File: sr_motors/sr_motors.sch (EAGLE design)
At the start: 20 parts

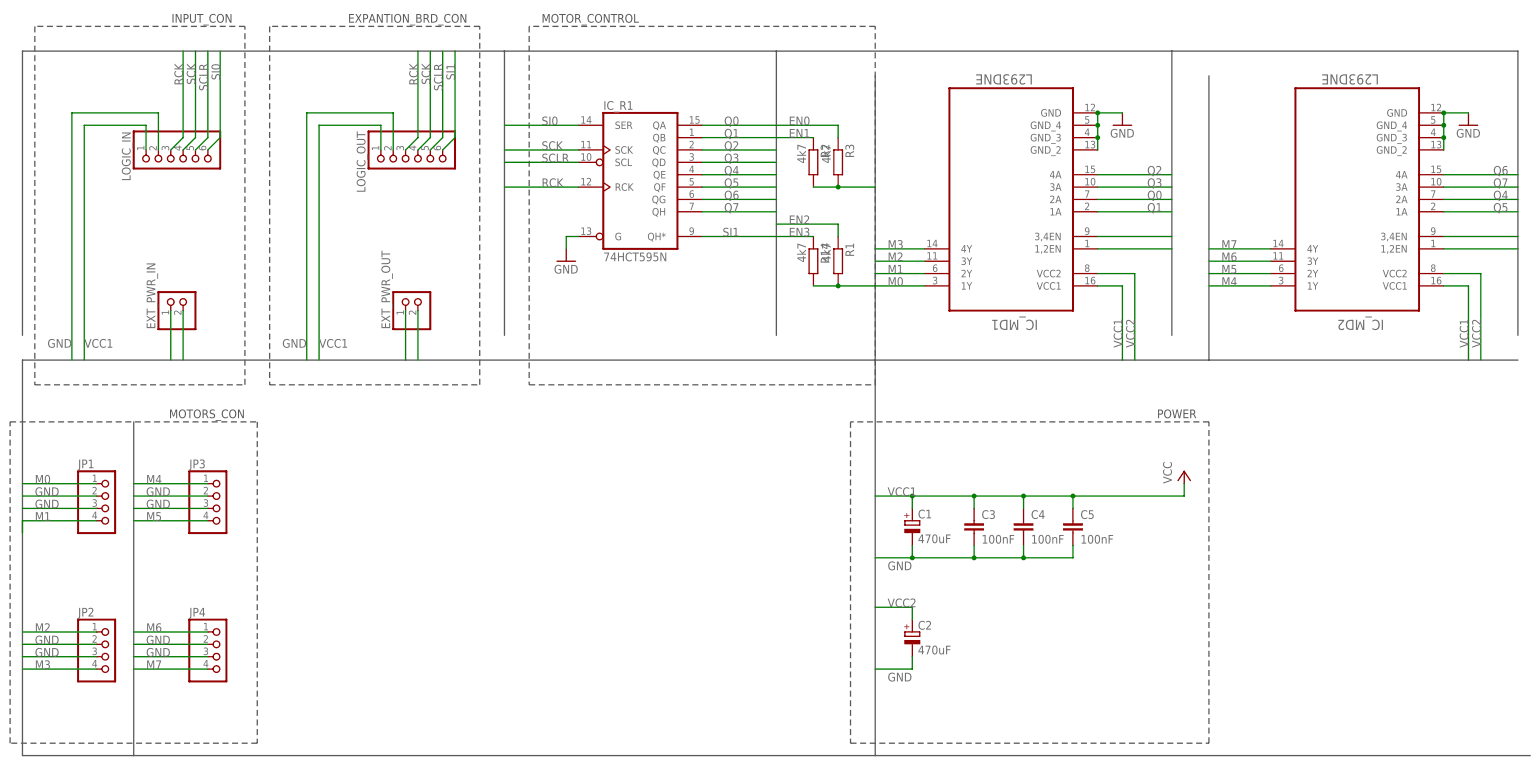
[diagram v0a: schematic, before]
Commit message: Added reverse current protection for external power, added version text
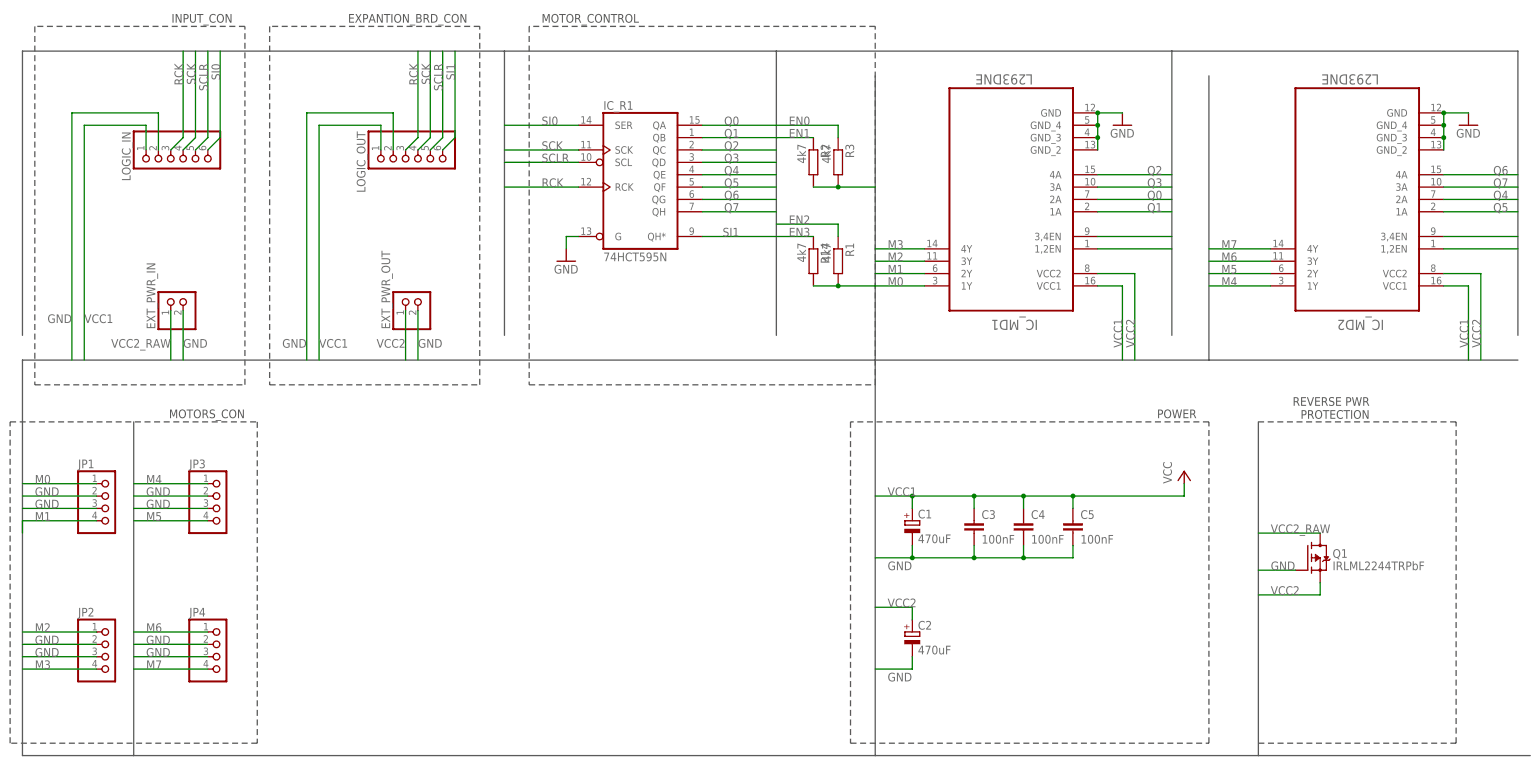
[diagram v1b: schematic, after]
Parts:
- added Q1: IRLML2244TRPbF, we-transistor:MOSFET-P-SOT23
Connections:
- new net VCC2_RAW: EXT_PWR_IN.1, Q1.D
- net GND: now also Q1.G
- net VCC2: now also Q1.S; no longer EXT_PWR_IN.1
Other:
- note added: "REVERSE PWR PROTECTION"
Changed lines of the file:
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@@
 <part name="JP3" library="pinhead" deviceset="PINHD-1X4" device=""/>
 <part name="JP4" library="pinhead" deviceset="PINHD-1X4" device=""/>
+<part name="Q1" library="we-transistor" deviceset="MOSFET-P" device="-SOT23" value="IRLML2244TRPbF"/>
 </parts>
 <sheets>
@@
 <text x="104.14" y="149.86" size="1.778" layer="97" rot="MR180">MOTOR_CONTROL</text>
 <text x="43.18" y="68.58" size="1.778" layer="97" rot="R180">MOTORS_CON</text>
+<wire x1="251.46" y1="0" x2="292.1" y2="0" width="0.1524" layer="97" style="shortdash"/>
+<wire x1="292.1" y1="0" x2="292.1" y2="66.04" width="0.1524" layer="97" style="shortdash"/>
+<wire x1="292.1" y1="66.04" x2="251.46" y2="66.04" width="0.1524" layer="97" style="shortdash"/>
+<text x="274.32" y="71.12" size="1.778" layer="97" rot="R180">REVERSE PWR
+PROTECTION</text>
 </plain>
 <instances>
@@
 <instance part="JP3" gate="A" x="38.1" y="48.26"/>
 <instance part="JP4" gate="A" x="38.1" y="17.78"/>
+<instance part="Q1" gate="T" x="264.16" y="38.1"/>
 </instances>
 <busses>
@@
 </segment>
 </bus>
-<bus name="OUTS:M[0..7],VCC1,VCC2,GND">
+<bus name="OUTS:M[0..7],VCC1,VCC2,GND,VCC2_RAW">
 <segment>
 <wire x1="172.72" y1="137.16" x2="172.72" y2="78.74" width="0.762" layer="92"/>
@@
 <wire x1="-2.54" y1="-2.54" x2="20.32" y2="-2.54" width="0.762" layer="92"/>
 <wire x1="20.32" y1="-2.54" x2="172.72" y2="-2.54" width="0.762" layer="92"/>
-<wire x1="172.72" y1="-2.54" x2="307.34" y2="-2.54" width="0.762" layer="92"/>
+<wire x1="172.72" y1="-2.54" x2="251.46" y2="-2.54" width="0.762" layer="92"/>
+<wire x1="251.46" y1="-2.54" x2="307.34" y2="-2.54" width="0.762" layer="92"/>
 <wire x1="20.32" y1="-2.54" x2="20.32" y2="66.04" width="0.762" layer="92"/>
+<wire x1="251.46" y1="-2.54" x2="251.46" y2="66.04" width="0.762" layer="92"/>
 </segment>
 <segment>
@@
 <pinref part="EXT_PWR_IN" gate="G$1" pin="2"/>
 <wire x1="30.48" y1="88.9" x2="30.48" y2="78.74" width="0.1524" layer="91"/>
+<label x="30.48" y="81.28" size="1.778" layer="95"/>
 </segment>
 <segment>
 <pinref part="EXT_PWR_OUT" gate="G$1" pin="2"/>
 <wire x1="78.74" y1="88.9" x2="78.74" y2="78.74" width="0.1524" layer="91"/>
+<label x="78.74" y="81.28" size="1.778" layer="95"/>
 </segment>
 <segment>
@@
 <wire x1="7.62" y1="129.54" x2="25.4" y2="129.54" width="0.1524" layer="91"/>
 <wire x1="7.62" y1="78.74" x2="7.62" y2="129.54" width="0.1524" layer="91"/>
-<label x="7.62" y="81.28" size="1.778" layer="95" rot="MR0"/>
+<label x="7.62" y="86.36" size="1.778" layer="95" rot="MR0"/>
 </segment>
 <segment>
@@
 <label x="22.86" y="48.26" size="1.778" layer="95"/>
 </segment>
+<segment>
+<pinref part="Q1" gate="T" pin="G"/>
+<wire x1="259.08" y1="35.56" x2="251.46" y2="35.56" width="0.1524" layer="91"/>
+<label x="254" y="35.56" size="1.778" layer="95"/>
+</segment>
 </net>
 <net name="SI0" class="0">
@@
 <net name="VCC2" class="1">
 <segment>
-<pinref part="EXT_PWR_IN" gate="G$1" pin="1"/>
-<wire x1="27.94" y1="88.9" x2="27.94" y2="78.74" width="0.1524" layer="91"/>
-</segment>
-<segment>
 <pinref part="EXT_PWR_OUT" gate="G$1" pin="1"/>
 <wire x1="76.2" y1="88.9" x2="76.2" y2="78.74" width="0.1524" layer="91"/>
+<label x="76.2" y="81.28" size="1.778" layer="95" rot="MR0"/>
 </segment>
 <segment>
@@
 <label x="297.18" y="81.28" size="1.778" layer="95" rot="R90"/>
 </segment>
+<segment>
+<pinref part="Q1" gate="T" pin="S"/>
+<wire x1="264.16" y1="33.02" x2="264.16" y2="30.48" width="0.1524" layer="91"/>
+<wire x1="251.46" y1="30.48" x2="264.16" y2="30.48" width="0.1524" layer="91"/>
+<label x="254" y="30.48" size="1.778" layer="95"/>
+</segment>
 </net>
 <net name="VCC1" class="2">
@@
 <wire x1="22.86" y1="121.92" x2="22.86" y2="127" width="0.1524" layer="91"/>
 <wire x1="10.16" y1="127" x2="22.86" y2="127" width="0.1524" layer="91"/>
-<label x="10.16" y="81.28" size="1.778" layer="95"/>
+<label x="10.16" y="86.36" size="1.778" layer="95"/>
 </segment>
 <segment>
@@
 </segment>
 </net>
+<net name="VCC2_RAW" class="0">
+<segment>
+<pinref part="Q1" gate="T" pin="D"/>
+<wire x1="264.16" y1="43.18" x2="251.46" y2="43.18" width="0.1524" layer="91"/>
+<label x="254" y="43.18" size="1.778" layer="95"/>
+</segment>
+<segment>
+<pinref part="EXT_PWR_IN" gate="G$1" pin="1"/>
+<wire x1="27.94" y1="88.9" x2="27.94" y2="78.74" width="0.1524" layer="91"/>
+<label x="27.94" y="81.28" size="1.778" layer="95" rot="MR0"/>
+</segment>
+</net>
 </nets>
 </sheet>
@@
 </schematic>
 </drawing>
+<compatibility>
+<note version="6.3" minversion="6.2.2" severity="warning">
+Since Version 6.2.2 text objects can contain more than one line,
+which will not be processed correctly with this version.
+</note>
+</compatibility>
 </eagle>
